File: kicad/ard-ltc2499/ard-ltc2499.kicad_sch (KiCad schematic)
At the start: 35 parts, among them P1 Power, P2 Analog, P3 Digital, P4 Digital, P5 CONN_01X01, P6 CONN_01X01, P7 CONN_01X01, P8 CONN_01X01

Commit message: Fixed 6654 symbol
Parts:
- gave numbers to parts that had none: 27
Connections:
- net VCC: now also U1.4 (VIN)
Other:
- moved on the sheet: C2

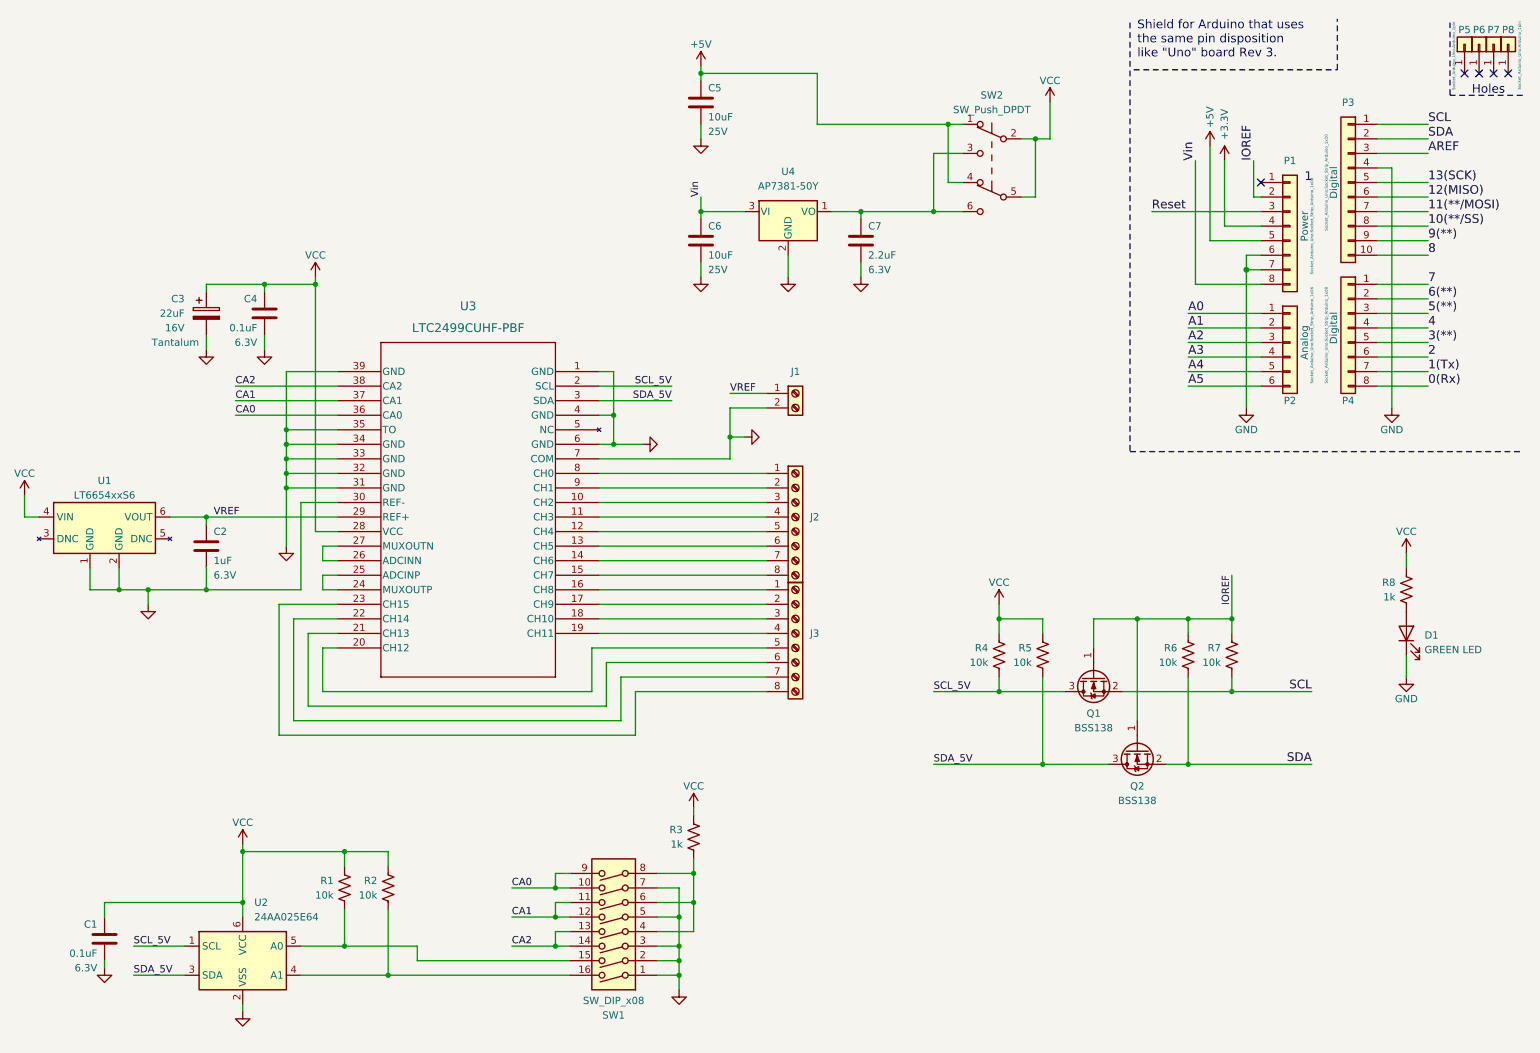
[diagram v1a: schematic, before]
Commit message: Added test points and individual address pull-ups
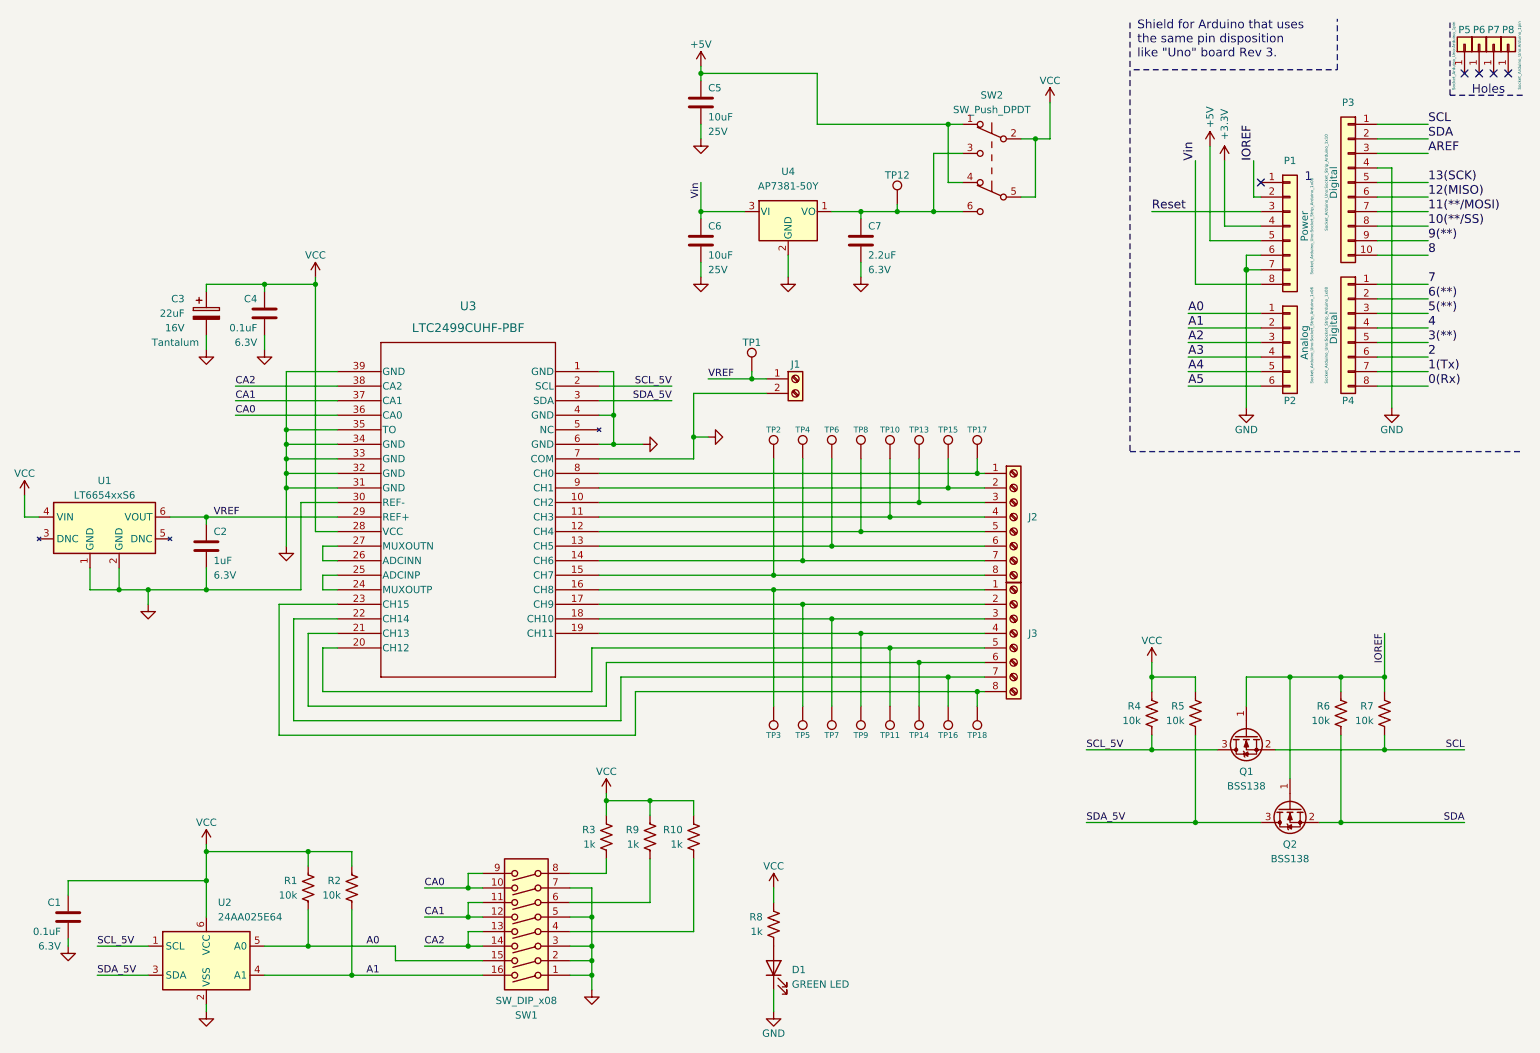
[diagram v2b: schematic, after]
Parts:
- added R10, R9: 1k, Resistor_SMD:R_0805_2012Metric, symbol Device:R_US
- added TP1, TP10, TP11, TP12, TP13, TP14, TP15, TP16, TP17, TP18, TP2, TP3, TP4, TP5, TP6, TP7, TP8, TP9: TestPoint, TestPoint:TestPoint_Pad_D2.0mm, symbol Connector:TestPoint
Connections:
- net A0: now also R1.1, SW1.15, U2.5 (A0)
- net A1: now also R2.1, SW1.16, U2.4 (A1)
- net VCC: now also R10.2, R9.2
- net VREF: now also TP1.1
- net at C7.1, SW2.3 (C), SW2.6 (C)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: now also TP12.1
- net at J3.1 (Pin_1), U3.16 (CH8): now also TP3.1
- net at J3.2 (Pin_2), U3.17 (CH9): now also TP5.1
- net at J3.3 (Pin_3), U3.18 (CH10): now also TP7.1
- net at J3.4 (Pin_4), U3.19 (CH11): now also TP9.1
- net at J3.5 (Pin_5), U3.20 (CH12): now also TP11.1
- net at J3.6 (Pin_6), U3.21 (CH13): now also TP14.1
- net at J3.7 (Pin_7), U3.22 (CH14): now also TP16.1
- net at J3.8 (Pin_8), U3.23 (CH15): now also TP18.1
- net at J2.1 (Pin_1), U3.8 (CH0): now also TP17.1
- net at J2.2 (Pin_2), U3.9 (CH1): now also TP15.1
- net at J2.3 (Pin_3), U3.10 (CH2): now also TP13.1
- net at J2.4 (Pin_4), U3.11 (CH3): now also TP10.1
- net at J2.5 (Pin_5), U3.12 (CH4): now also TP8.1
- net at J2.6 (Pin_6), U3.13 (CH5): now also TP6.1
- net at J2.7 (Pin_7), U3.14 (CH6): now also TP4.1
- net at J2.8 (Pin_8), U3.15 (CH7): now also TP2.1
- net at R3.1, SW1.8: no longer SW1.4, SW1.6
- new net: R10.1, SW1.4
- new net: R9.1, SW1.6
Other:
- moved on the sheet: C1, D1, J1, J2, J3, Q1, Q2, R1, R2, R3, R4, R5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

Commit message: Initial placement
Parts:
- SW2: value SW_Push_DPDT -> JS202011SCQN
- TP1, TP10, TP11, TP12, TP13, TP14, TP15, TP16, TP17, TP18, TP2, TP3, TP4, TP5, TP6, TP7, TP8, TP9: footprint TestPoint:TestPoint_Pad_D2.0mm -> TestPoint:TestPoint_Pad_D1.5mm
- renumbered U3 to U1, U1 to U2, U4 to U3, U2 to U4

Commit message: Complete PCB
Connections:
- net A0: no longer R1.1, SW1.15, U4.5 (A0)
- net A1: no longer R2.1, SW1.16, U4.4 (A1)
- net CA0: now also SW1.5, SW1.6; no longer SW1.10, SW1.9
- net CA1: now also SW1.3, SW1.4; no longer SW1.11, SW1.12
- net CA2: now also SW1.1, SW1.2; no longer SW1.13, SW1.14
- net GND: now also SW1.10, SW1.11, SW1.13, SW1.15, SW1.9; no longer P3.4 (Pin_4), SW1.1, SW1.2, SW1.3, SW1.5, SW1.7
- net at R10.1: now also SW1.12; no longer SW1.4
- net at R3.1: now also SW1.16; no longer SW1.8
- net at R9.1: now also SW1.14; no longer SW1.6
- new net AD0: R1.1, SW1.8, U4.5 (A0)
- new net AD1: R2.1, SW1.7, U4.4 (A1)
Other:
- moved on the sheet: SW1
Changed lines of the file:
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@@
     (stroke (width 0) (type default) (color 0 0 0 0))
   )
-  (wire (pts (xy 87.63 176.53) (xy 87.63 173.99))
+  (wire (pts (xy 87.63 179.07) (xy 87.63 173.99))
     (stroke (width 0) (type default) (color 0 0 0 0))
   )
@@
   )
   (wire (pts (xy 68.58 91.44) (xy 77.47 91.44))
-    (stroke (width 0) (type default) (color 0 0 0 0))
-  )
-  (wire (pts (xy 102.87 176.53) (xy 87.63 176.53))
     (stroke (width 0) (type default) (color 0 0 0 0))
   )
@@
     (stroke (width 0) (type default) (color 0 0 0 0))
   )
-  (wire (pts (xy 80.01 179.07) (xy 102.87 179.07))
-    (stroke (width 0) (type default) (color 0 0 0 0))
-  )
   (wire (pts (xy 74.93 104.14) (xy 74.93 106.68))
     (stroke (width 0) (type default) (color 0 0 0 0))
@@
     (stroke (width 0) (type default) (color 0 0 0 0))
   )
+  (wire (pts (xy 87.63 179.07) (xy 102.87 179.07))
+    (stroke (width 0) (type default) (color 0 0 0 0))
+  )
   (wire (pts (xy 259.08 43.18) (xy 267.97 43.18))
     (stroke (width 0) (type solid) (color 0 0 0 0))
@@
   (wire (pts (xy 189.23 91.44) (xy 123.19 91.44))
     (stroke (width 0) (type default) (color 0 0 0 0))
-  )
-  (wire (pts (xy 261.62 38.1) (xy 261.62 80.01))
-    (stroke (width 0) (type solid) (color 0 0 0 0))
   )
   (wire (pts (xy 100.33 166.37) (xy 100.33 168.91))
@@
     (stroke (width 0) (type solid) (color 0 0 0 0))
   )
+  (wire (pts (xy 80.01 179.07) (xy 85.09 179.07))
+    (stroke (width 0) (type default) (color 0 0 0 0))
+  )
   (wire (pts (xy 227.33 58.42) (xy 227.33 36.83))
     (stroke (width 0) (type solid) (color 0 0 0 0))
@@
   )
   (wire (pts (xy 73.66 58.42) (xy 73.66 101.6))
+    (stroke (width 0) (type default) (color 0 0 0 0))
+  )
+  (wire (pts (xy 85.09 176.53) (xy 102.87 176.53))
     (stroke (width 0) (type default) (color 0 0 0 0))
   )
@@
     (stroke (width 0) (type solid) (color 0 0 0 0))
   )
+  (wire (pts (xy 85.09 179.07) (xy 85.09 176.53))
+    (stroke (width 0) (type default) (color 0 0 0 0))
+  )
   (wire (pts (xy 129.54 129.54) (xy 129.54 137.16))
     (stroke (width 0) (type default) (color 0 0 0 0))
@@
     (effects (font (size 1.524 1.524)) (justify left bottom))
   )
-  (label "CA2" (at 92.71 173.99 0)
+  (label "CA0" (at 92.71 173.99 0)
     (effects (font (size 1.27 1.27)) (justify left bottom))
   )
@@
     (effects (font (size 1.524 1.524)) (justify left bottom))
   )
-  (label "A1" (at 82.55 179.07 0)
+  (label "AD1" (at 74.93 179.07 0)
     (effects (font (size 1.27 1.27)) (justify left bottom))
   )
@@
     (effects (font (size 1.524 1.524)) (justify left bottom))
   )
-  (label "A0" (at 82.55 173.99 0)
+  (label "AD0" (at 74.93 173.99 0)
     (effects (font (size 1.27 1.27)) (justify left bottom))
   )
@@
     (effects (font (size 1.27 1.27)) (justify right bottom))
   )
-  (label "CA0" (at 92.71 163.83 0)
+  (label "CA2" (at 92.71 163.83 0)
     (effects (font (size 1.27 1.27)) (justify left bottom))
   )
@@
     (property "Footprint" "" (id 2) (at 236.22 80.01 0))
     (property "Datasheet" "" (id 3) (at 236.22 80.01 0))
-    (pin "1")
-  )
-  (symbol (lib_id "power:GND") (at 261.62 80.01 0) (unit 1)
-    (in_bom yes) (on_board yes)
-    (property "Reference" "#PWR04" (id 0) (at 261.62 86.36 0)
-      (effects (font (size 1.27 1.27)) hide)
-    )
-    (property "Value" "GND" (id 1) (at 261.62 83.82 0))
-    (property "Footprint" "" (id 2) (at 261.62 80.01 0))
-    (property "Datasheet" "" (id 3) (at 261.62 80.01 0))
     (pin "1")
   )
@@
     (pin "9")
   )
-  (symbol (lib_id "Switch:SW_DIP_x08") (at 110.49 168.91 180) (unit 1)
-    (in_bom yes) (on_board yes)
-    (property "Reference" "SW1" (id 0) (at 110.49 186.055 0))
-    (property "Value" "SW_DIP_x08" (id 1) (at 110.49 183.515 0))
-    (property "Footprint" "Button_Switch_SMD:SW_DIP_SPSTx08_Slide_6.7x21.88mm_W8.61mm_P2.54mm_LowProfile" (id 2) (at 110.49 168.91 0)
-      (effects (font (size 1.27 1.27)) hide)
-    )
-    (property "Datasheet" "~" (id 3) (at 110.49 168.91 0)
+  (symbol (lib_id "Switch:SW_DIP_x08") (at 110.49 171.45 0) (unit 1)
+    (in_bom yes) (on_board yes)
+    (property "Reference" "SW1" (id 0) (at 110.49 154.305 0))
+    (property "Value" "SW_DIP_x08" (id 1) (at 110.49 156.845 0))
+    (property "Footprint" "Button_Switch_SMD:SW_DIP_SPSTx08_Slide_6.7x21.88mm_W8.61mm_P2.54mm_LowProfile" (id 2) (at 110.49 171.45 0)
+      (effects (font (size 1.27 1.27)) hide)
+    )
+    (property "Datasheet" "~" (id 3) (at 110.49 171.45 0)
       (effects (font (size 1.27 1.27)) hide)
     )
@@
       (reference "#PWR03") (unit 1) (value "GND") (footprint "")
     )
-    (path "/00000000-0000-0000-0000-000056d70cff"
-      (reference "#PWR04") (unit 1) (value "GND") (footprint "")
-    )
     (path "/b61b095a-5616-4540-9dc7-1452ba9d86f0"
